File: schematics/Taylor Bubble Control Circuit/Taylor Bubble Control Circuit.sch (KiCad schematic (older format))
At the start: 14 parts, among them J1 Banana Plug, J2 Banana Plug, J3 Conn_01x02, J4 Conn_01x03, U1 STM32 Nucleo F446RE Board, U2 L7805CV-DG, U3 TL062

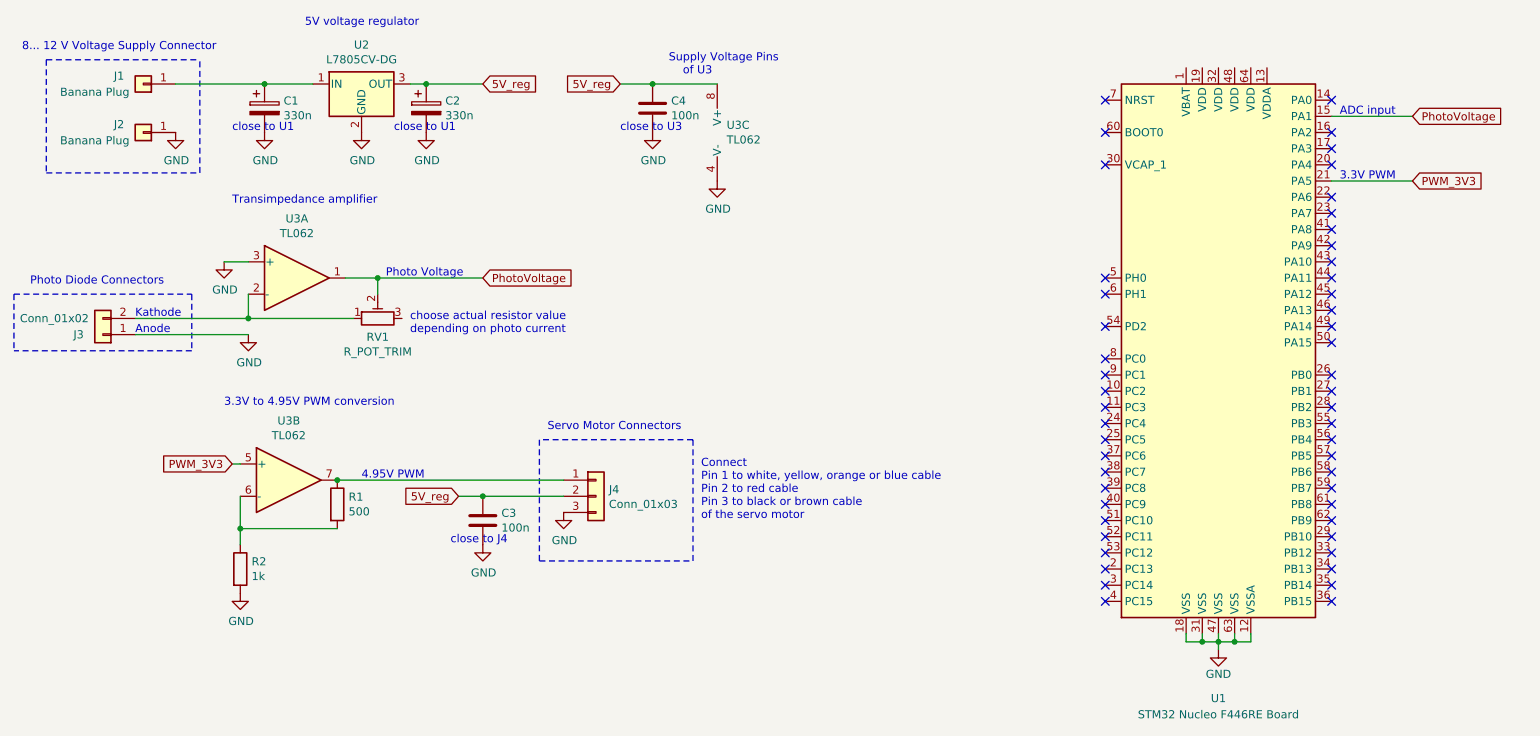
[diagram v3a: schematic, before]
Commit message: updated schematics
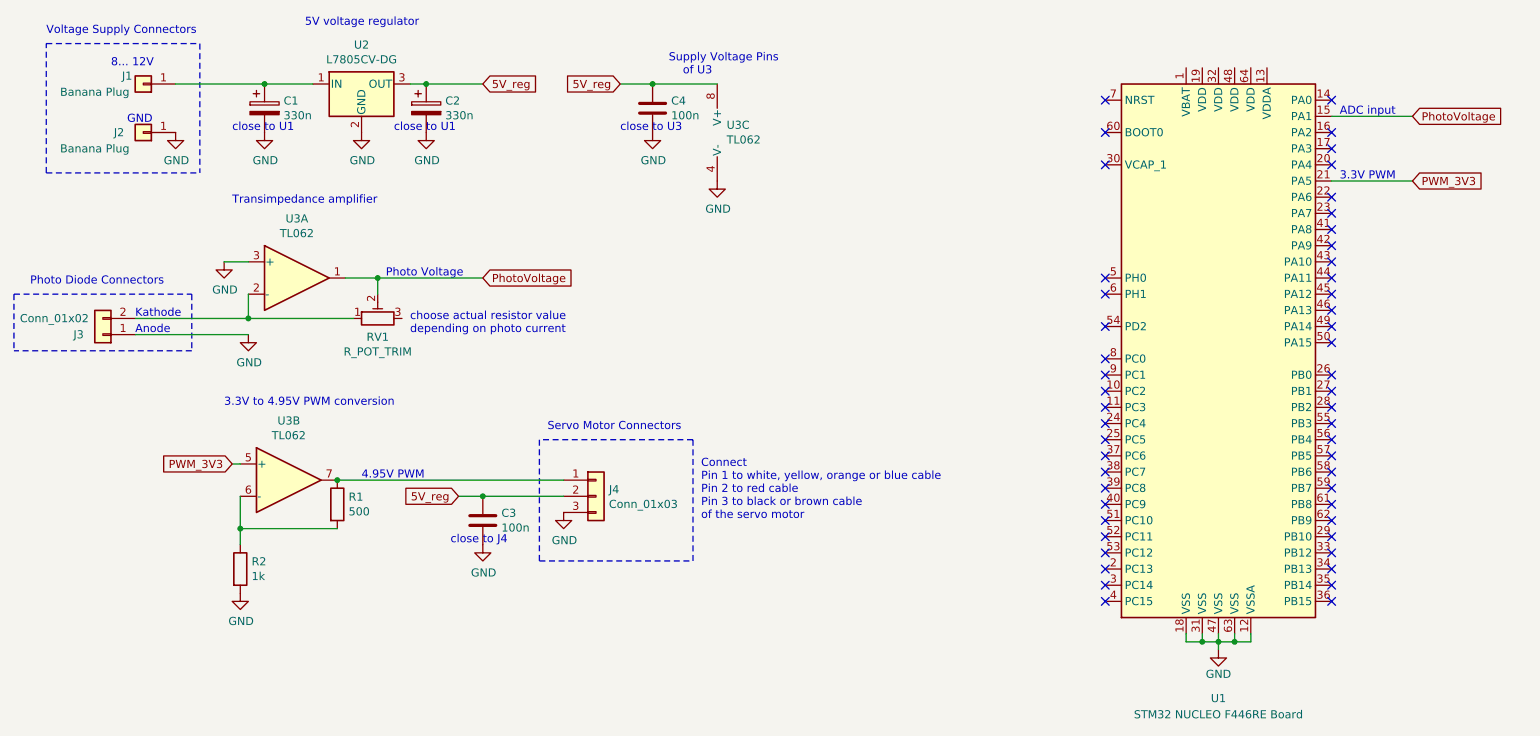
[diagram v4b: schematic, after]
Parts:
- U1: value STM32 Nucleo F446RE Board -> STM32 NUCLEO F446RE Board
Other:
- note added: "8... 12V"
- note added: "GND"
- note added: "Voltage Supply Connectors\n"
- note removed: "8... 12 V Voltage Supply Connector\n"
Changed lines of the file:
@@
 U 1 1 62D22786
 P 2000 1350
-F 0 "J1" H 2150 1300 50  0000 C CNN
+F 0 "J1" H 2100 1300 50  0000 C CNN
 F 1 "Banana Plug" H 2300 1400 50  0000 C CNN
 F 2 "" H 2000 1350 50  0001 C CNN
@@
 P 8650 2950
 F 0 "U1" H 8650 750 50  0000 C CNN
-F 1 "STM32 Nucleo F446RE Board" H 8650 650 50  0000 C CNN
+F 1 "STM32 NUCLEO F446RE Board" H 8650 650 50  0000 C CNN
 F 2 "Package_QFP:LQFP-64_10x10mm_P0.5mm" H 8050 1250 50  0001 R CNN
 F 3 "https://www.st.com/resource/en/user_manual/um1724-stm32-nucleo64-boards-mb1136-stmicroelectronics.pdf" H 8650 2950 50  0001 C CNN
@@
 Text Notes 2500 3350 0    50   ~ 0
 3.3V to 4.95V PWM conversion
-Text Notes 1250 1150 0    50   ~ 0
-8... 12 V Voltage Supply Connector\n
+Text Notes 1400 1050 0    50   ~ 0
+Voltage Supply Connectors\n
 Text Notes 5250 1300 0    50   ~ 0
 Supply Voltage Pins \n    of U3
@@
 U 1 1 62D04412
 P 2000 1650
-F 0 "J2" H 2150 1600 50  0000 C CNN
-F 1 "Banana Plug" H 2300 1700 50  0000 C CNN
+F 0 "J2" H 2150 1650 50  0000 C CNN
+F 1 "Banana Plug" H 2300 1750 50  0000 C CNN
 F 2 "" H 2000 1650 50  0001 C CNN
 F 3 "~" H 2000 1650 50  0001 C CNN
@@
 Wire Notes Line
 	1400 1900 2350 1900
-Wire Notes Line
-	2350 1900 2350 1200
-Wire Notes Line
-	1400 1200 2350 1200
-Wire Notes Line
-	1400 1200 1400 1900
+Text Notes 1800 1250 0    50   ~ 0
+8... 12V
+Text Notes 1900 1600 0    50   ~ 0
+GND
+Wire Notes Line
+	1400 1100 2350 1100
+Wire Notes Line
+	2350 1100 2350 1900
+Wire Notes Line
+	1400 1900 1400 1100
 $EndSCHEMATC

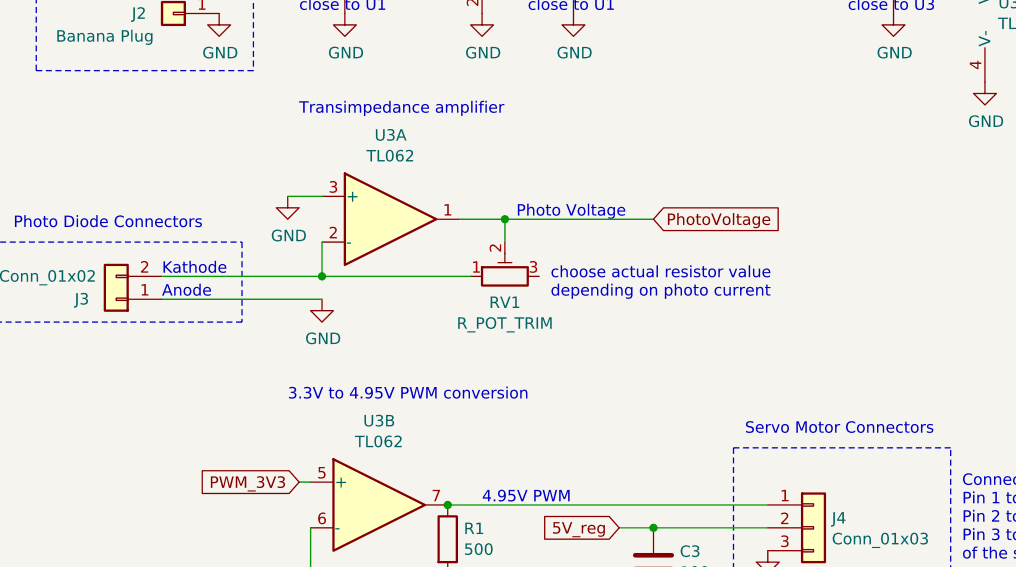
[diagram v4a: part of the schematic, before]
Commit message: updated schematics
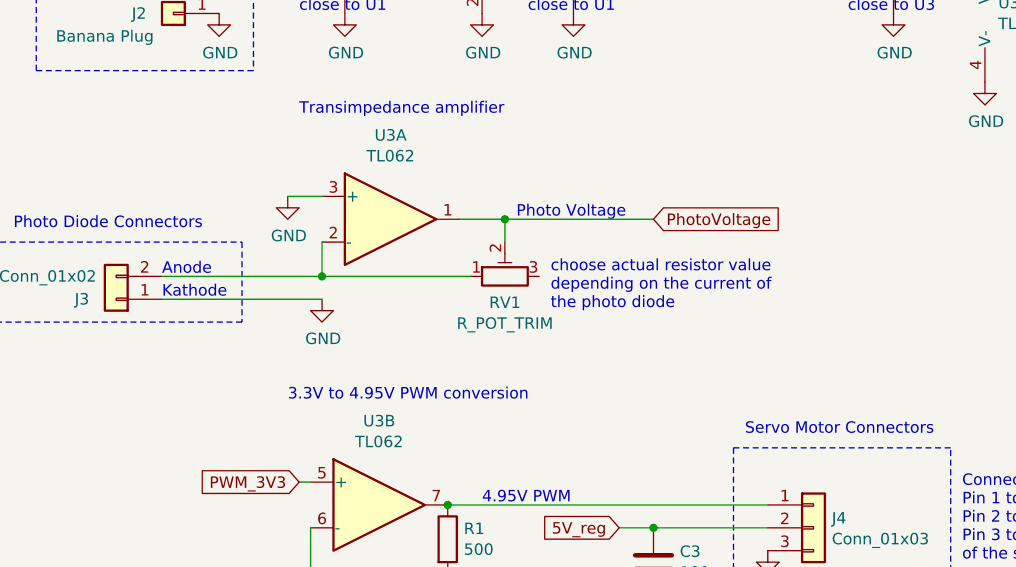
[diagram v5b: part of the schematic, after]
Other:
- note added: "choose actual resistor value \ndepending on the current of \nthe photo diode"
- note removed: "choose actual resistor value \ndepending on photo current"
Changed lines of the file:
@@
 Text Notes 3500 2550 0    50   ~ 0
 Photo Voltage
+Text Notes 1950 2900 0    50   ~ 0
+Kathode
 Text Notes 1950 2800 0    50   ~ 0
-Kathode
-Text Notes 1950 2900 0    50   ~ 0
 Anode
 Wire Wire Line
@@
 Text Notes 3000 1000 0    50   ~ 0
 5V voltage regulator
-Text Notes 3650 2900 0    50   ~ 0
-choose actual resistor value \ndepending on photo current
+Text Notes 3650 2950 0    50   ~ 0
+choose actual resistor value \ndepending on the current of \nthe photo diode
 $Comp
 L Device:R_POT_TRIM RV1
